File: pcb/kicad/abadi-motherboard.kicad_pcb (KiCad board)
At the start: 2 copper layers, 100 x 100 mm, 44 parts, among them J1 ESP32-S3 J1 (lower row), J3 ESP32-S3 J3 (upper row)

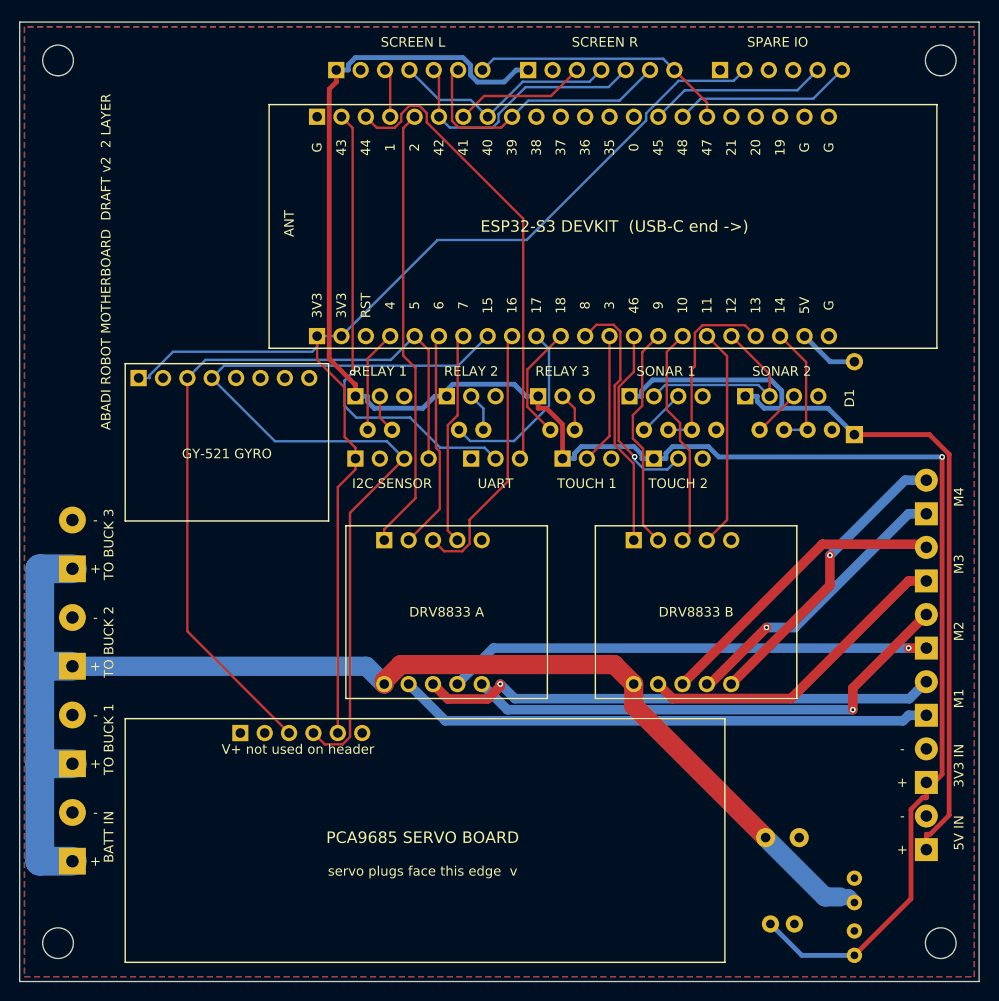
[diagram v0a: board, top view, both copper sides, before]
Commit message: Rebuild the robot motherboard as v3 from the paper test-fit
Footprints now follow the measured ESP32-S3 board (57 x 28 mm, rows 25.4 mm
apart), the PCA9685 header on its short end and the GY-521 pin order.
Touch headers removed, all screw terminals 5.08 mm, 3-way power input for
the bucks. Silkscreen now marks polarity and values (C1/C2, D1, resistors)
and prints pin functions beside every cable header. Screen headers are
2.54 mm apart and the antenna keep-out is larger.

Fully routed on 2 layers. KiCad DRC shows 0 errors / 0 unconnected, and the
independent Gerber audit finds 0 shorts / 0 opens (176 plated holes matched).
The audit now also lists which pads sit in a split net.

Co-Authored-By: Claude Sonnet 5.5 <noreply@anthropic.com>
Claude-Session: https://claude.ai/code/session_01FTMr77tNTaQwRQC74wgVC1
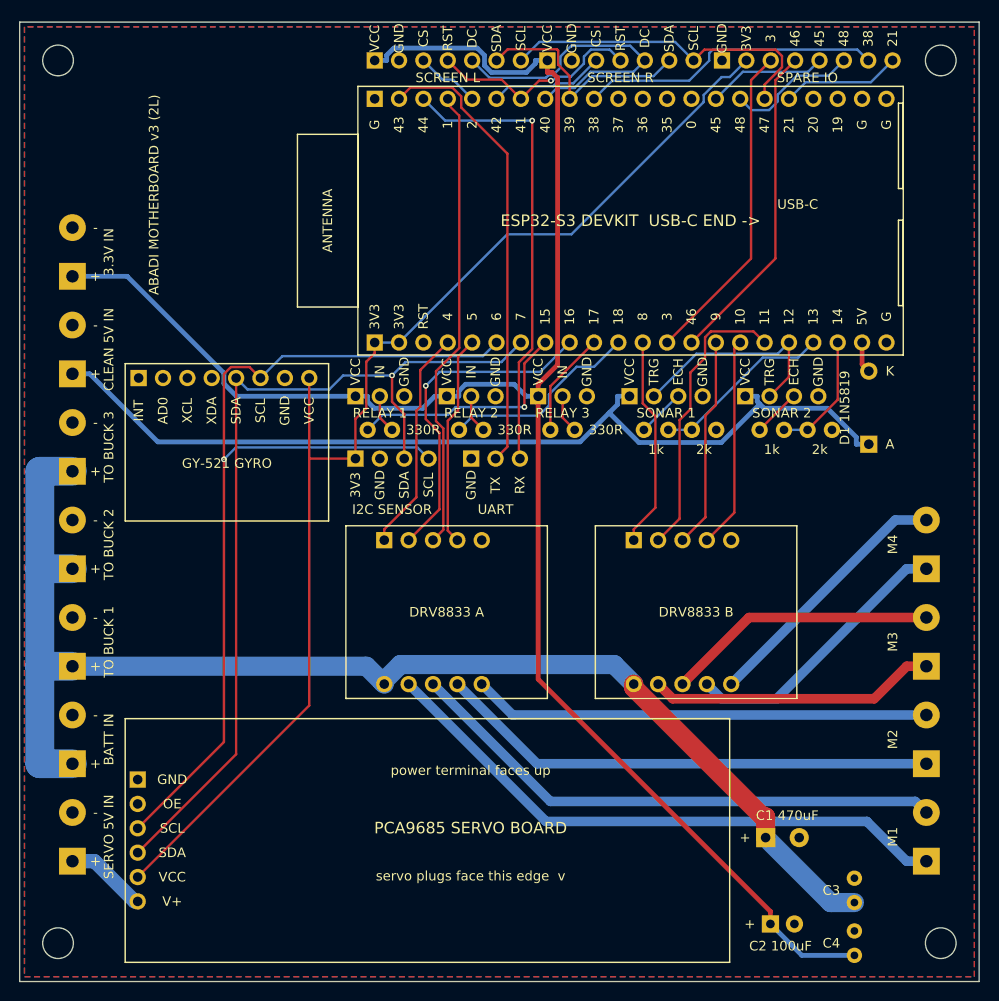
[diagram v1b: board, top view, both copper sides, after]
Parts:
- removed TCH1: TOUCH 1, abadi:FP_TCH1
- removed TCH2: TOUCH 2, abadi:FP_TCH2
- removed TR_33: 3.3V IN, abadi:FP_TR_33
- removed TR_5V: CLEAN 5V IN, abadi:FP_TR_5V
- added TL4: TO BUCK 3, abadi:FP_TL4, F.Cu at (105.5, 96.8)
- added TL5: CLEAN 5V IN, abadi:FP_TL5, F.Cu at (105.5, 86.7)
- added TL6: 3.3V IN, abadi:FP_TL6, F.Cu at (105.5, 76.5)
- GYRO: value GY-521 -> GY-521 (INT AD0 XCL XDA SDA SCL GND VCC)
- J1: value ESP32-S3 J1 (lower row) -> ESP32-S3 row 1 (3V3 RST 4 5 ...)
- J3: value ESP32-S3 J3 (upper row) -> ESP32-S3 row 2 (GND TX RX 1 2 ...)
- PCA: value PCA9685 control (GND OE SCL SDA VCC V+) -> PCA9685 header (GND OE SCL SDA VCC V+)
- TL0: value BATT IN -> SERVO 5V IN
- TL1: value TO BUCK 1 -> BATT IN
- TL2: value TO BUCK 2 -> TO BUCK 1
- TL3: value TO BUCK 3 -> TO BUCK 2
- moved TM1 15.2 mm to (194.5, 137.5)
- moved TM2 12.0 mm to (194.5, 127.3)
- moved PCA 11.7 mm to (112.3, 128.9)
- moved TM3 8.89 mm to (194.5, 117.1)
- moved J3 6.28 mm to (137.0, 58.0)
- moved J1 6.04 mm to (137.0, 83.4)
- moved TM4 5.73 mm to (194.5, 107.0)
- moved SCR_L 4.12 mm to (137.0, 54.0)
- moved SCR_R 2.24 mm to (155.0, 54.0)
- moved D1 1.80 mm to (188.5, 94.0)
- moved SPARE 1.02 mm to (173.2, 54.0)
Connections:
- GYRO pad 1: ESP3V3 -> (no net)
- GYRO pad 2: GND -> (no net)
- GYRO pad 3: SCL -> (no net)
- GYRO pad 4: SDA -> (no net)
- GYRO pad 5: (no net) -> SDA
- GYRO pad 6: (no net) -> SCL
- GYRO pad 7: (no net) -> GND
- GYRO pad 8: (no net) -> ESP3V3
- J1 pad 10: RLY2 -> RLY3
- J1 pad 11: RLY3 -> RLY2
- J1 pad 13: TOUCH1 -> SPARE3
- J1 pad 14: TOUCH2 -> SPARE46
- J1 pad 15: IN2B -> IN3B
- J1 pad 16: IN3B -> IN4B
- J1 pad 17: IN4B -> IN2B
- J1 pad 4: RLY1 -> IN1A
- J1 pad 5: SCL -> IN4A
- J1 pad 6: IN2A -> SCL
- J1 pad 7: IN4A -> SDA
- J1 pad 8: SDA -> RLY1
- J1 pad 9: IN3A -> IN2A
- J3 pad 18: (no net) -> SPARE21
- J3 pad 4: CS_L -> IN3A
- J3 pad 5: IN1A -> CS_L
- J3 pad 6: LCD_DC -> CS_R
- J3 pad 7: CS_R -> LCD_RST
- J3 pad 8: LCD_RST -> LCD_DC
- PCA pad 6: (no net) -> SERVO5
- TL0 pad 1: VBAT -> SERVO5
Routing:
- net SPARE3: track 0.00 -> 33.9 mm
- net SPARE46: track 0.00 -> 33.9 mm
- net SPARE38: track 0.00 -> 31.6 mm
- net SCL: track 80.3 -> 104.1 mm, vias 0 -> 1
- net IN1A: track 46.5 -> 23.3 mm
- net IN3A: track 28.1 -> 48.3 mm
- net TOUCH2: track 19.7 -> 0.00 mm, vias 1 -> 0
- net RLY1: track 10.7 -> 24.9 mm, vias 0 -> 1
- net TOUCH1: track 13.7 -> 0.00 mm
- net SPARE21: track 0.00 -> 12.5 mm
- net CLEAN5: track 85.7 -> 97.8 mm
- net IN2A: track 22.9 -> 34.9 mm, vias 0 -> 1
- net SERVO5: track 0.00 -> 8.54 mm
- net RAILC: track 198.0 -> 190.0 mm, vias 1 -> 0
- net SCK: track 27.3 -> 34.8 mm
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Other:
- board text added: "1k"
- board text added: "2k"
- board text added: "3.3V IN"
- board text added: "330R"
- board text added: "A"
- board text added: "ABADI MOTHERBOARD v3 (2L)"
- board text added: "AD0"
- board text added: "ANTENNA"
- board text added: "C1 470uF"
- board text added: "C2 100uF"
- board text added: "C3"
- board text added: "C4"
- board text added: "CLEAN 5V IN"
- board text added: "CS"
- board text added: "D1 1N5819"
- board text added: "DC"
- board text added: "ECH"
- board text added: "ESP32-S3 DEVKIT USB-C END ->"
- board text added: "GND"
- board text added: "IN"
- board text added: "INT"
- board text added: "K"
- board text added: "OE"
- board text added: "RX"
- board text added: "SCL"
- board text added: "SDA"
- board text added: "SERVO 5V IN"
- board text added: "TRG"
- board text added: "TX"
- board text added: "USB-C"
- board text added: "V+"
- board text added: "VCC"
- board text added: "XCL"
- board text added: "XDA"
- board text added: "power terminal faces up"
- board text removed: "3V3 IN"
- board text removed: "5V IN"
- board text removed: "ABADI ROBOT MOTHERBOARD DRAFT v2 2 LAYER"
- board text removed: "ANT"
- board text removed: "D1"
- board text removed: "ESP32-S3 DEVKIT (USB-C end ->)"
- board text removed: "TOUCH 1"
- board text removed: "TOUCH 2"
- board text removed: "V+ not used on header"

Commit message: Motherboard v4: battery feeds the bucks outside the board, add POWER OUT header
The three TO BUCK terminals are removed. The buck modules now take their
battery power straight from the pack (off-board splice and fuse), and the
board only has BATT IN (motors) plus the three buck outputs coming back in:
SERVO 5V IN, CLEAN 5V IN and 3.3V IN.

New POWER OUT header on the left edge: 2 x clean 5 V, 2 x 3.3 V (from the
3.3 V buck, not the ESP32's own pin) and 4 x GND, each power pin with a
ground pin below it. README gets a "How to wire the power" section.

Routed on 2 layers: KiCad DRC 0 errors / 0 unconnected; independent Gerber
audit 0 shorts / 0 opens (177 plated holes matched). Still a draft: do not
order before the paper test-fit.

Co-Authored-By: Claude Sonnet 5.5 <noreply@anthropic.com>
Claude-Session: https://claude.ai/code/session_01FTMr77tNTaQwRQC74wgVC1
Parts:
- removed TL4: TO BUCK 3, abadi:FP_TL4
- removed TL5: CLEAN 5V IN, abadi:FP_TL5
- removed TL6: 3.3V IN, abadi:FP_TL6
- added PWR: POWER OUT (5V 5V 3V3 3V3 / GND x4), abadi:FP_PWR, F.Cu at (106.0, 111.5)
- TL2: value TO BUCK 1 -> CLEAN 5V IN
- TL3: value TO BUCK 2 -> 3.3V IN
- moved TL2 30.5 mm to (105.5, 86.7)
- moved TL3 30.5 mm to (105.5, 76.5)
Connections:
- TL2 pad 1: VBAT -> CLEAN5
- TL3 pad 1: VBAT -> RAILC
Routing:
- net RAILC: track 190.0 -> 218.7 mm, vias 0 -> 1
- net CLEAN5: track 97.8 -> 124.6 mm
- net VBAT: track 139.0 -> 116.4 mm
- net M1A: track 61.6 -> 75.2 mm
- net LCD_DC: track 33.5 -> 21.3 mm
- net SDA: track 95.1 -> 105.9 mm, vias 1 -> 0
- net IN3A: track 48.3 -> 57.6 mm
- net SCL: track 104.1 -> 111.7 mm, vias 1 -> 0
- net SPARE3: track 33.9 -> 40.5 mm
- net UART_RX: track 48.1 -> 41.7 mm, vias 1 -> 0
- net UART_TX: track 47.6 -> 41.7 mm
- net M3B: track 28.3 -> 32.4 mm, vias 0 -> 1
- net TRIG: track 22.8 -> 19.4 mm
- net RLY1: track 24.9 -> 28.3 mm, vias 1 -> 0
- net MOSI: track 24.5 -> 21.3 mm
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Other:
- board text added: "ABADI MOTHERBOARD v4 (2L)"
- board text added: "POWER OUT"
- board text removed: "ABADI MOTHERBOARD v3 (2L)"
- board text removed: "TO BUCK 1"
- board text removed: "TO BUCK 2"
- board text removed: "TO BUCK 3"

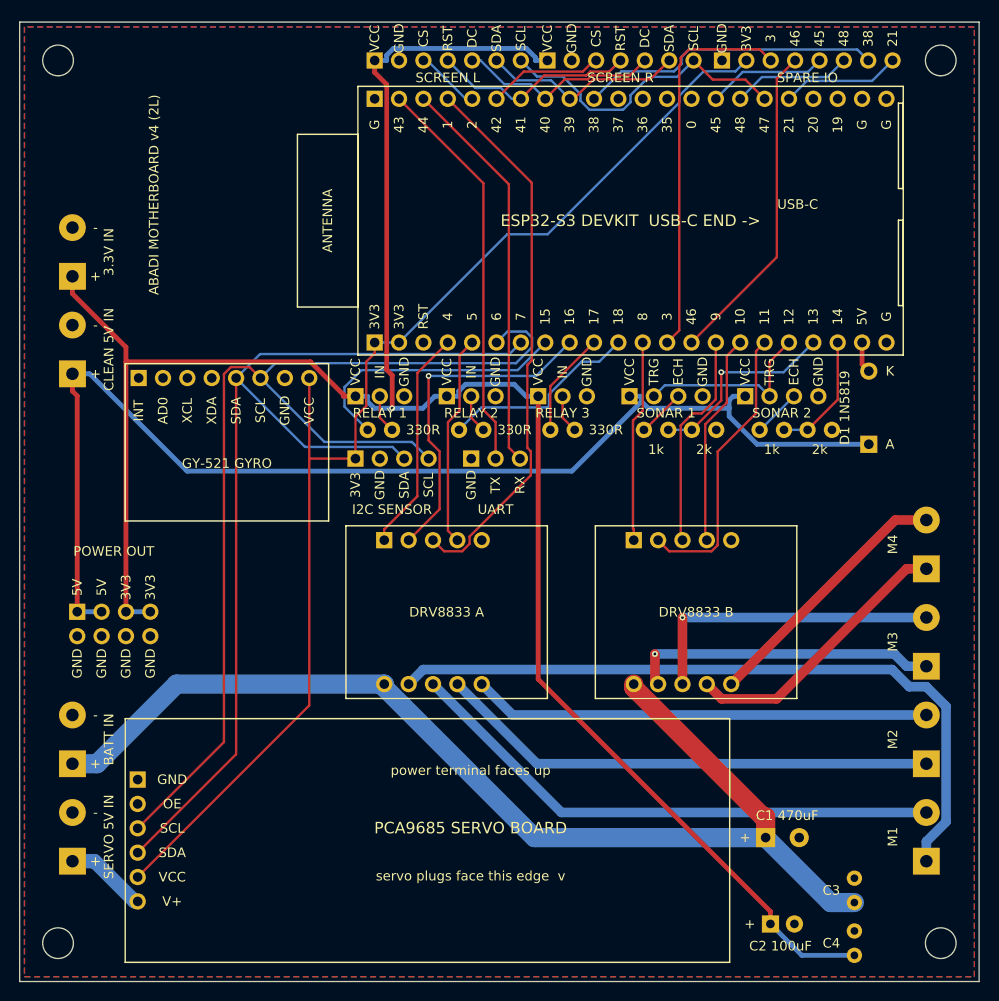
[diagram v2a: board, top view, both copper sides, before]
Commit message: Motherboard v4: remove relay series resistors, loosen the header layout
The relay modules are 3 V types with their own input circuit, so each relay
header's IN pin now connects straight to its ESP32 pin (three resistors and
their holes removed). The cable headers are spaced 3 mm apart, the I2C and
UART headers moved up 2 mm, and diode D1 moved to the right of the sonar
strip. The sonar echo dividers stay (ESP32-S3 pins are not 5 V tolerant).

Routed on 2 layers: KiCad DRC 0 errors / 0 unconnected; independent Gerber
audit 0 shorts / 0 opens (177 plated holes matched).

Co-Authored-By: Claude Sonnet 5.5 <noreply@anthropic.com>
Claude-Session: https://claude.ai/code/session_01FTMr77tNTaQwRQC74wgVC1
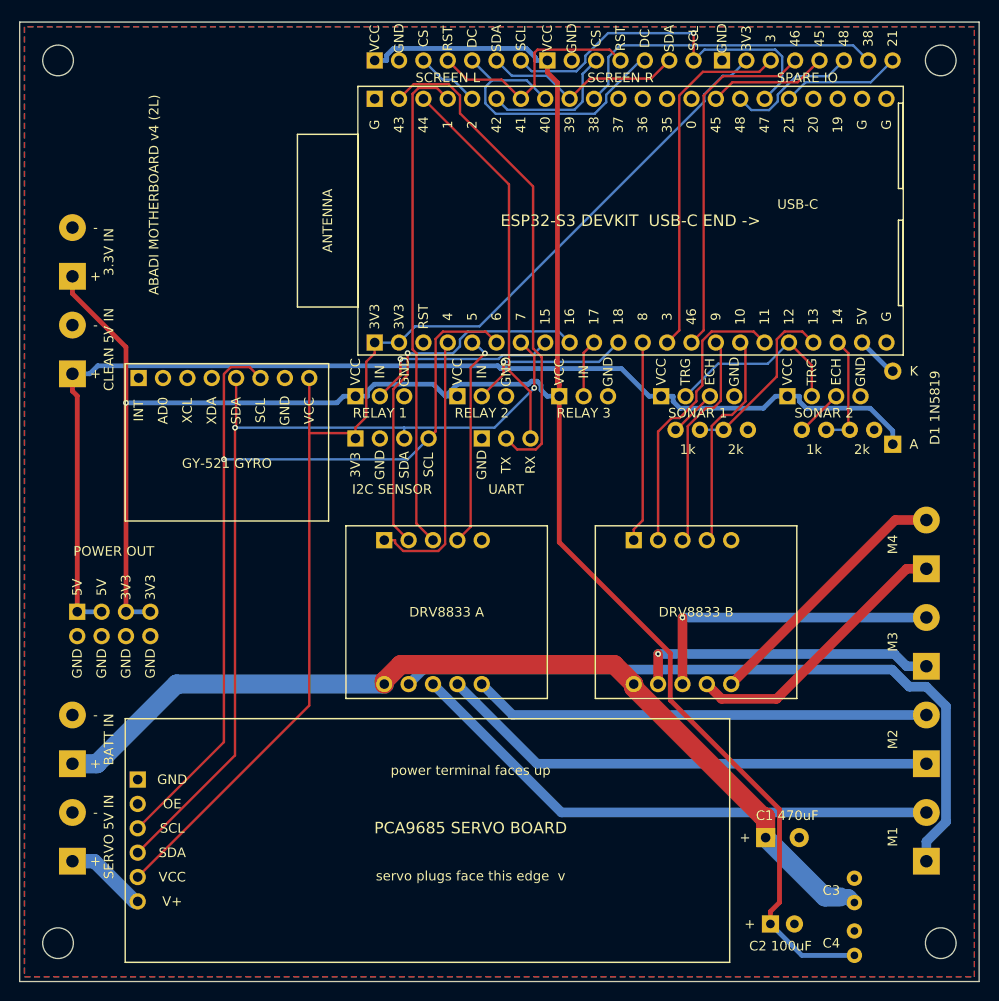
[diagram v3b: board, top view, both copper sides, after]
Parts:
- removed RS1: 330R, abadi:FP_RS1
- removed RS2: 330R, abadi:FP_RS2
- removed RS3: 330R, abadi:FP_RS3
- moved RD2a 4.40 mm to (181.5, 92.5)
- moved RD2b 4.40 mm to (186.5, 92.5)
- moved SON2 4.40 mm to (180.0, 89.0)
- moved RD1a 3.30 mm to (168.4, 92.5)
- moved RD1b 3.30 mm to (173.4, 92.5)
- moved SON1 3.30 mm to (166.9, 89.0)
- moved D1 2.50 mm to (191.0, 94.0)
- moved UART 2.37 mm to (148.2, 93.4)
- moved RLY3H 2.20 mm to (156.2, 89.0)
- moved I2C 2.10 mm to (135.0, 93.4)
- moved RLY2H 1.10 mm to (145.6, 89.0)
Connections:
- RLY1H pad 2: RLY1_H -> RLY1
- RLY2H pad 2: RLY2_H -> RLY2
- RLY3H pad 2: RLY3_H -> RLY3
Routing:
- net VBAT: track 116.4 -> 97.7 mm
- net SCL: track 111.7 -> 95.7 mm, vias 0 -> 1
- net SDA: track 105.9 -> 93.1 mm, vias 0 -> 2
- net LCD_DC: track 21.3 -> 31.8 mm
- net UART_TX: track 41.7 -> 51.7 mm
- net RLY1: track 28.3 -> 20.6 mm, vias 0 -> 1
- net SCK: track 32.2 -> 38.5 mm, vias 0 -> 1
- net IN3A: track 57.6 -> 51.8 mm
- net CLEAN5: track 124.6 -> 119.3 mm
- net IN1A: track 23.3 -> 28.4 mm
- net RLY3: track 11.0 -> 6.05 mm
- net IN2A: track 35.1 -> 39.5 mm
- net RLY2_H: track 4.03 -> 0.00 mm
- net RLY1_H: track 4.03 -> 0.00 mm
- net RLY3_H: track 4.03 -> 0.00 mm
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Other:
- board text removed: "330R"

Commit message: Motherboard v4: motor connectors become 2-pin JST spots, DRV pin names printed
M1-M4 are now 2-pin positions on a 2.54 mm grid for the owner's 2-pin JST
plugs instead of 5.08 mm screw terminals. The DRV8833 holes now print their
pin names (IN1..IN4, GND, VM, motor outputs) so they can be compared with the
module's own labels. Header spacing is 2.8 mm (a ground pad was walled in
at 3.0 mm; the Gerber audit caught it).

Routed on 2 layers: KiCad DRC 0 errors / 0 unconnected; independent Gerber
audit 0 shorts / 0 opens (172 plated holes matched).

Co-Authored-By: Claude Sonnet 5.5 <noreply@anthropic.com>
Claude-Session: https://claude.ai/code/session_01FTMr77tNTaQwRQC74wgVC1
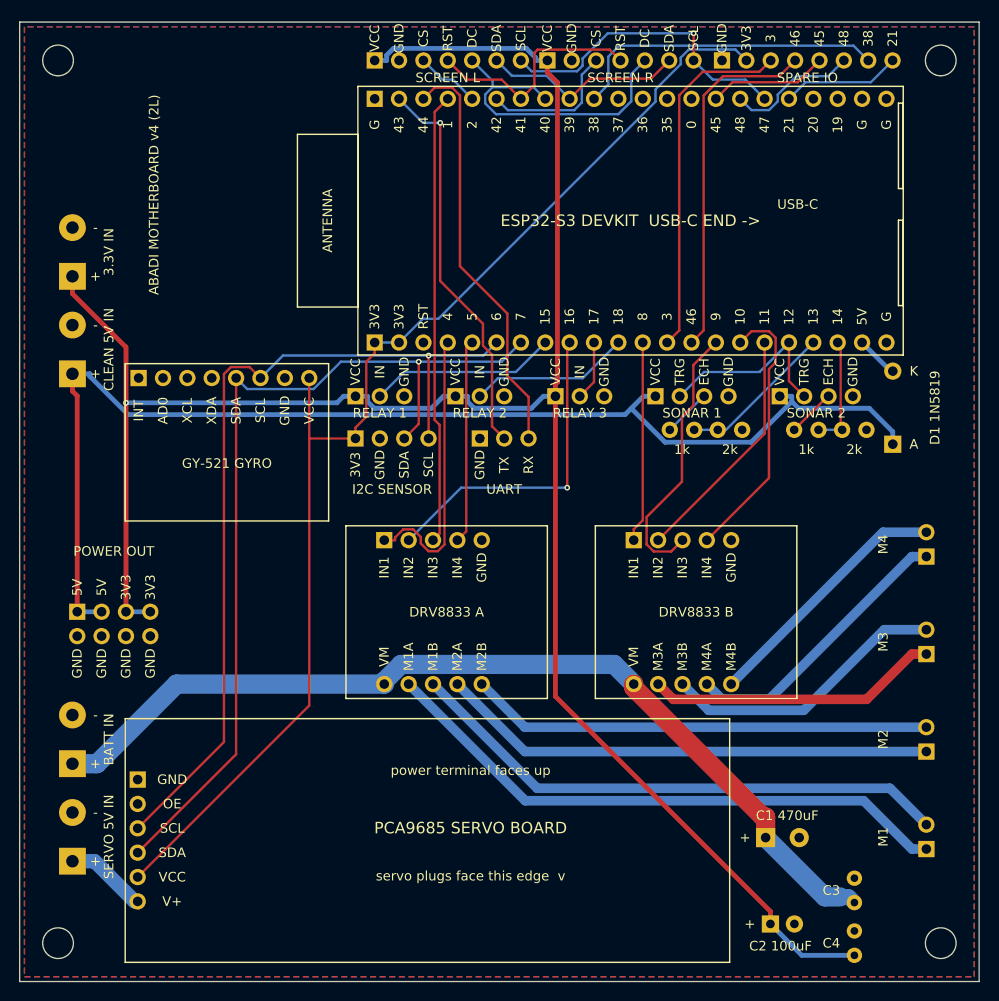
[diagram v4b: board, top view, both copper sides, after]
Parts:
- TM1: value MOTOR 1 -> MOTOR 1 (2-pin JST)
- TM2: value MOTOR 2 -> MOTOR 2 (2-pin JST)
- TM3: value MOTOR 3 -> MOTOR 3 (2-pin JST)
- TM4: value MOTOR 4 -> MOTOR 4 (2-pin JST)
- moved TM1 1.27 mm to (194.5, 136.2)
- moved TM2 1.27 mm to (194.5, 126.0)
- moved TM3 1.27 mm to (194.5, 115.9)
- moved TM4 1.27 mm to (194.5, 105.7)
- moved RD2a 0.80 mm to (180.7, 92.5)
- moved RD2b 0.80 mm to (185.7, 92.5)
- moved SON2 0.80 mm to (179.2, 89.0)
- moved RD1a 0.60 mm to (167.8, 92.5)
- moved RD1b 0.60 mm to (172.8, 92.5)
- moved SON1 0.60 mm to (166.3, 89.0)
- moved RLY3H 0.40 mm to (155.8, 89.0)
- moved RLY2H 0.20 mm to (145.4, 89.0)
- moved UART 0.20 mm to (148.0, 93.4)
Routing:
- net M1A: track 75.2 -> 61.1 mm
- net UART_TX: track 51.7 -> 41.0 mm, vias 0 -> 1
- net CLEAN5: track 119.3 -> 125.9 mm
- net SCK: track 38.5 -> 32.4 mm
- net IN3B: track 22.9 -> 28.6 mm
- net IN2A: track 39.5 -> 34.0 mm
- net IN4B: track 23.0 -> 28.5 mm
- net IN2B: track 30.5 -> 25.2 mm
- net SCL: track 95.7 -> 90.4 mm
- net IN3A: track 51.8 -> 47.1 mm
- net UART_RX: track 40.0 -> 43.4 mm
- net ECHO1_3V: track 18.8 -> 16.2 mm
- net RAILC: track 219.5 -> 217.0 mm
- net M3B: track 32.4 -> 30.0 mm, vias 1 -> 0
- net ESP3V3: track 126.4 -> 128.1 mm
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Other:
- board text added: "IN1"
- board text added: "IN2"
- board text added: "IN3"
- board text added: "IN4"
- board text added: "M1A"
- board text added: "M1B"
- board text added: "M2A"
- board text added: "M2B"
- board text added: "M3A"
- board text added: "M3B"
- board text added: "M4A"
- board text added: "M4B"
- board text added: "VM"
